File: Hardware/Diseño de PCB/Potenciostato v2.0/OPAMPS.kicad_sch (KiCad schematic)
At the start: 29 parts, among them IC1 LMP7702MAX_NOPB, IC2 LMP7701MFX_NOPB, IC3 LMP7701MFX_NOPB, U1 MAX4737EUD+, U2 LMP7721MA/NOPB, U4 MAX5491LA01000+T, U5 MAX4617CSE+

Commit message: Big commit. Hardware was already ready. Board arrived. Hardware testing phase and software development is ongoing, some hardware issues were detected and noted down in the KiCad project for future versions and design corrections. First software libraries under development for ADC, GPIO, Muxes and DAC managment (ADS1255, MAX5217, MAX4737, MAX4617 and GPIO)
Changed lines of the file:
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@@
 	)
 	(hierarchical_label "CE"
-		(shape input)
+		(shape output)
 		(at 91.44 66.04 180)
 		(fields_autoplaced yes)

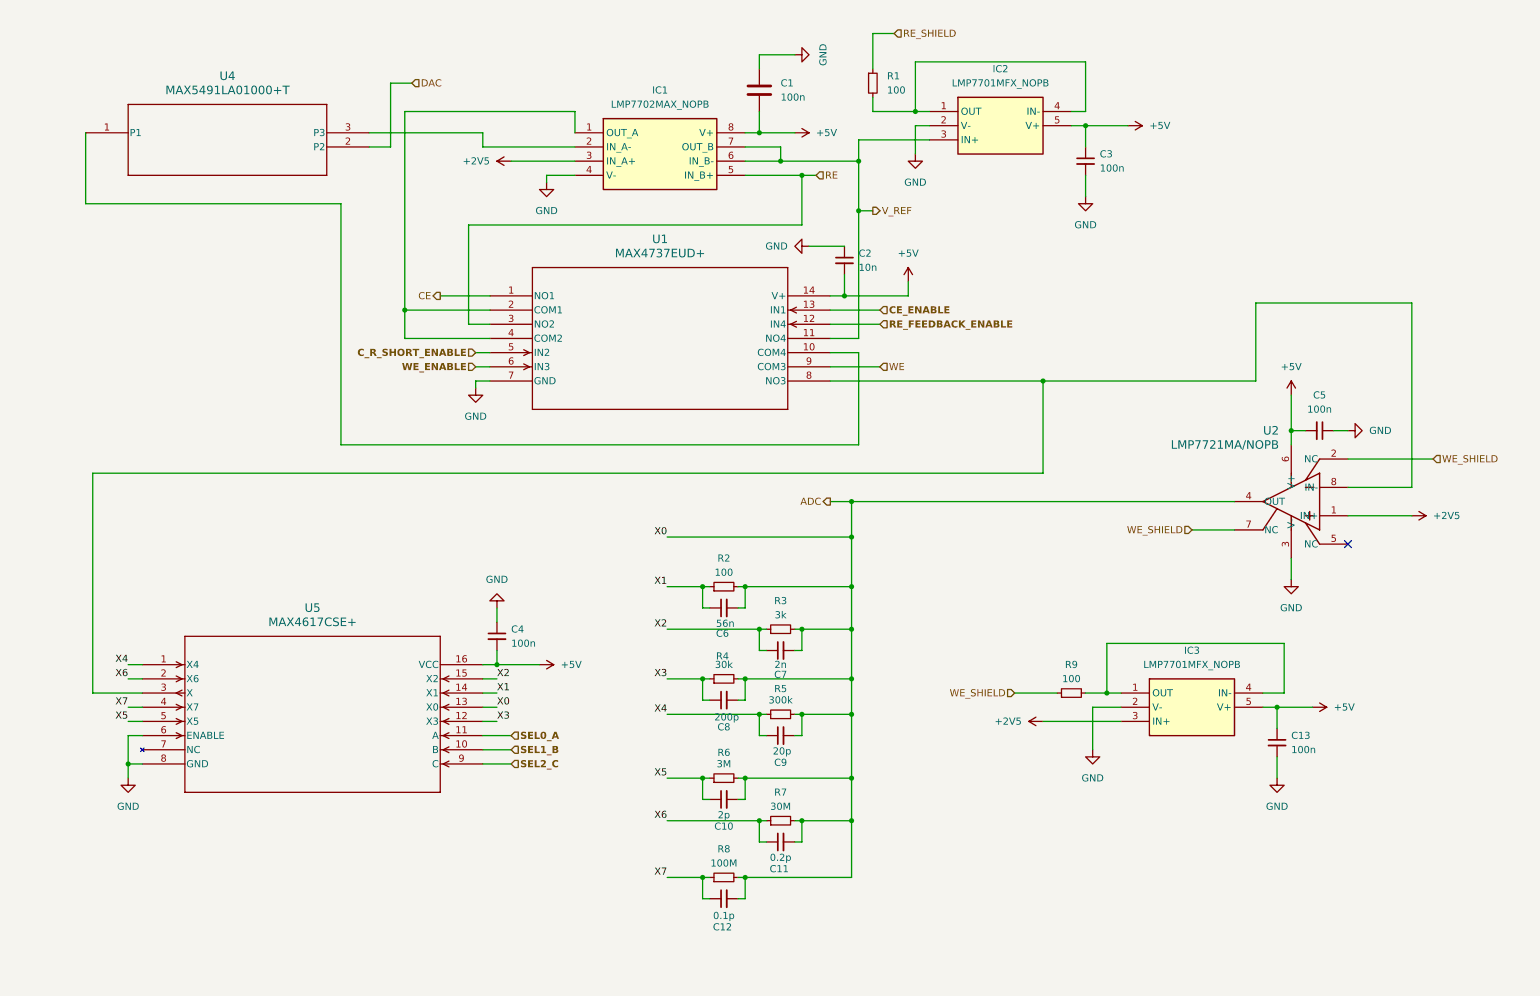
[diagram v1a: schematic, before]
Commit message: Further documentation and notes on the schematic. Software updates: In MAX4617, corrections in write function, more robust code verification to prevent overflows. In MUX, correction to MAX4617 gain codification and pinout updgraded for MAX4737. ADS1255, mux configured to AIN0-AINCOM in ADS_Initialized.
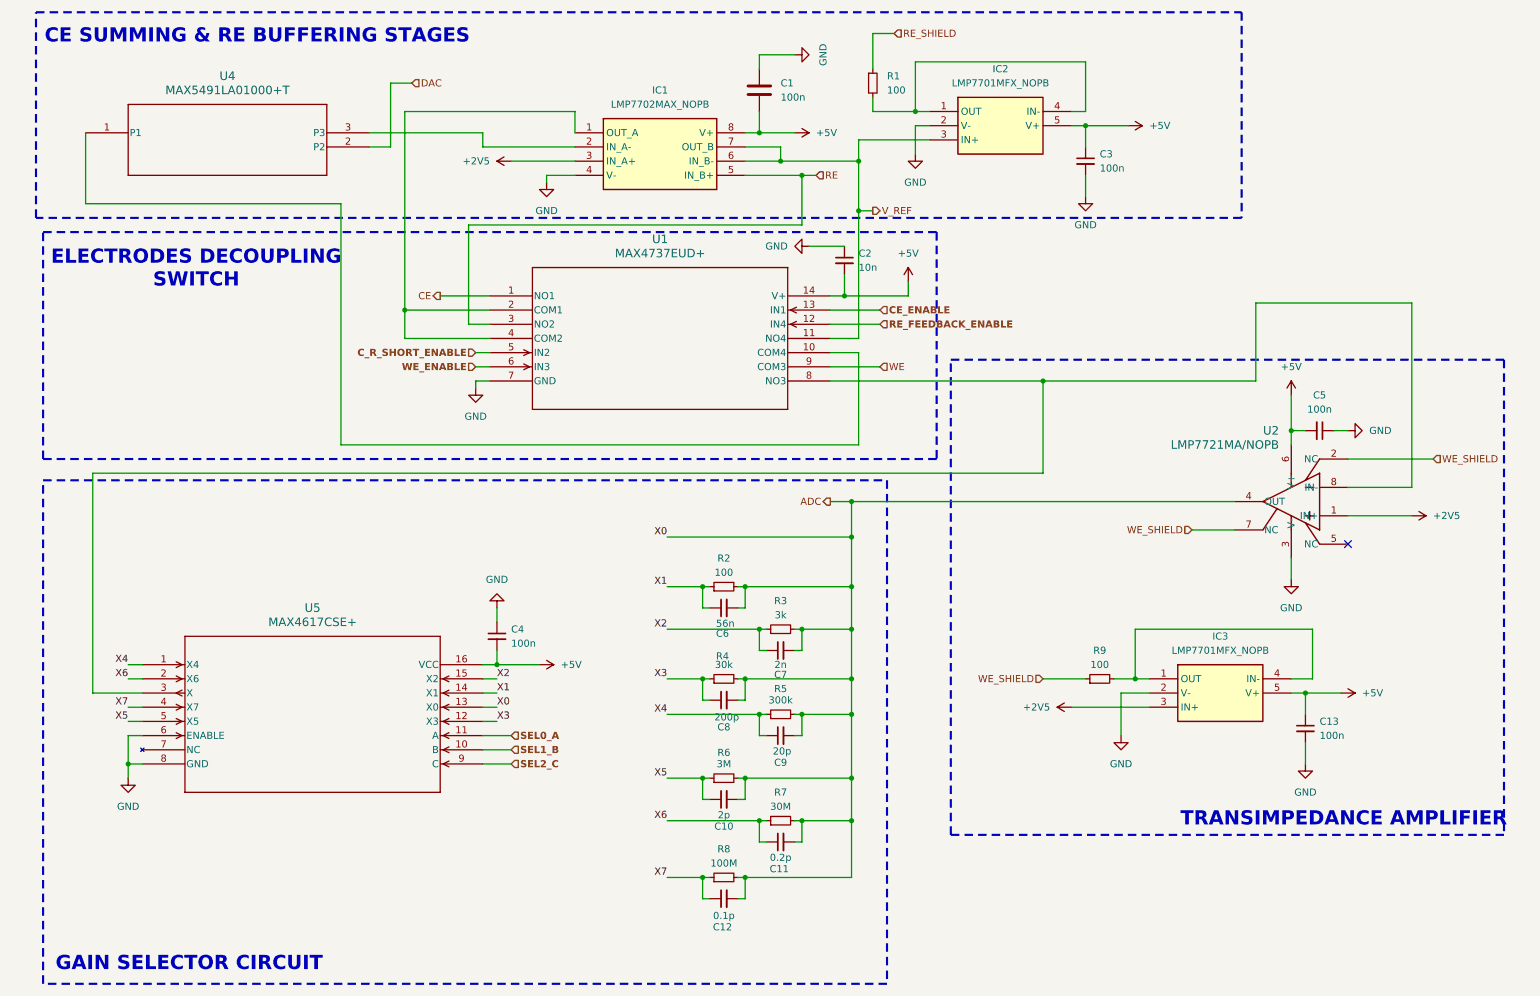
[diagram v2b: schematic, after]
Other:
- note added: "CE SUMMING & RE BUFFERING STAGES"
- note added: "ELECTRODES DECOUPLING SWITCH"
- note added: "GAIN SELECTOR CIRCUIT"
- note added: "TRANSIMPEDANCE AMPLIFIER"
- moved on the sheet: C13, IC3, R9

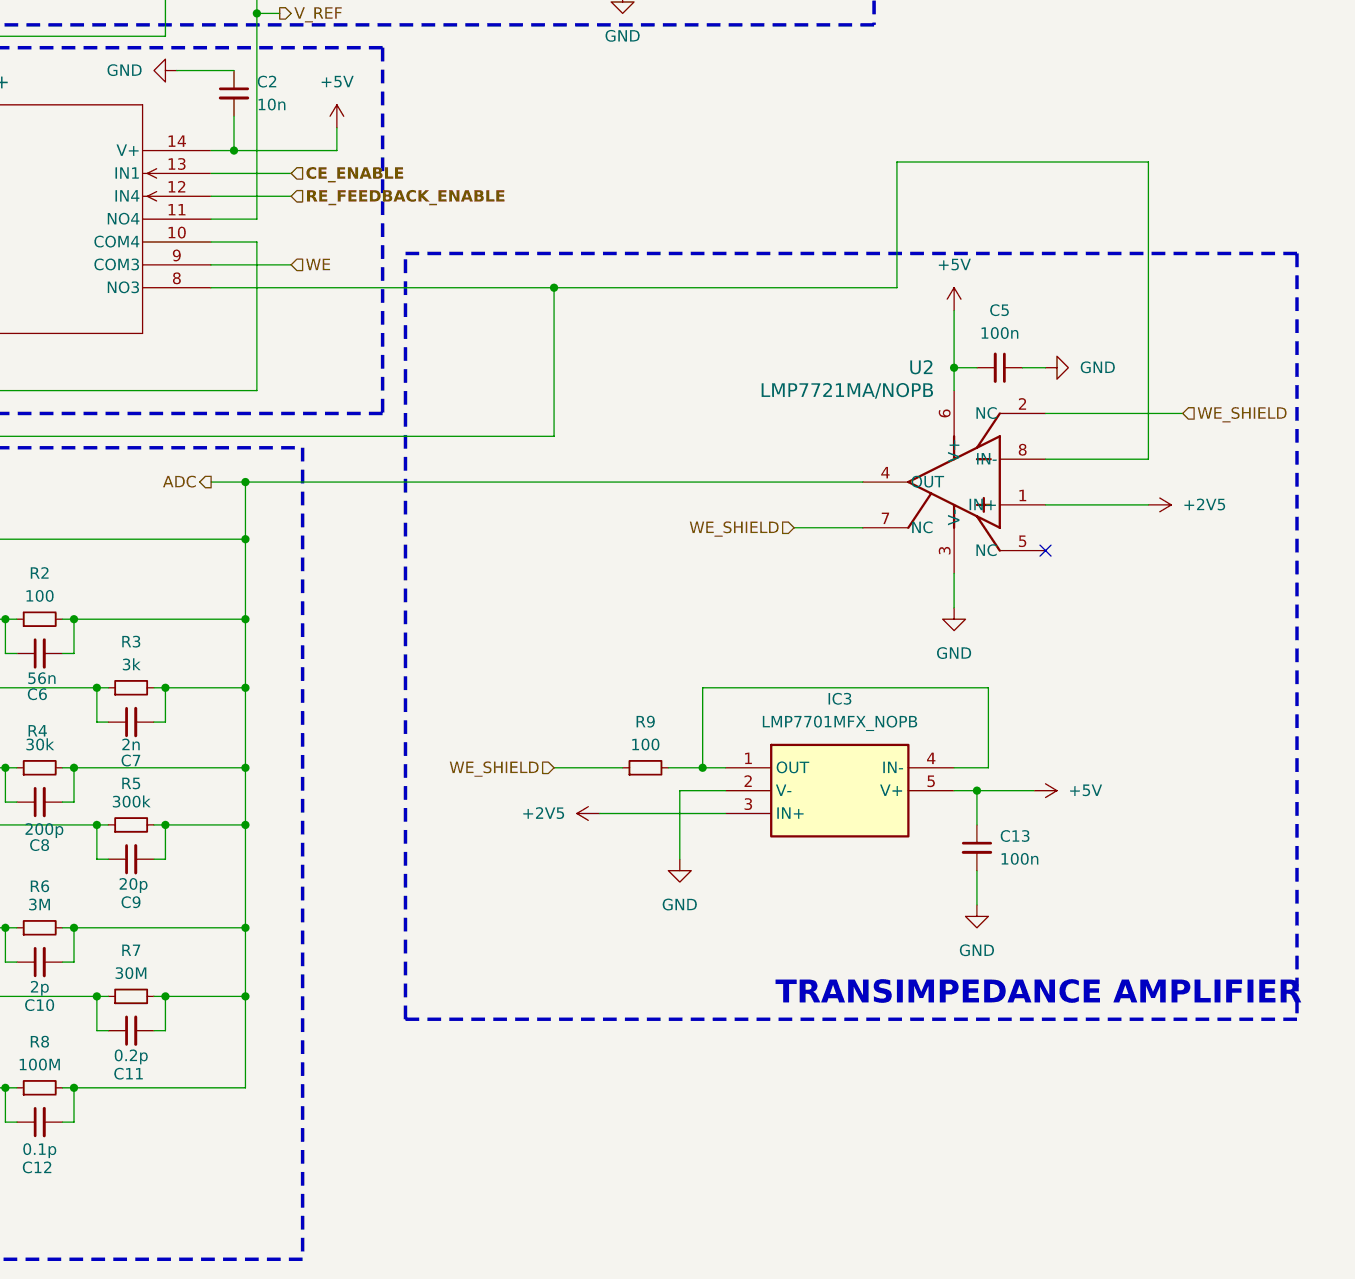
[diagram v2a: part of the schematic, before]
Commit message: Hardware: Hardware Corrections in Potentiostat, small but important ones (WE electrode, Normal Open connection for electric disconnection in schematic and PCB. DAC I2C pull up resistors connected to 5V PCB layout corrected.). New project for ESP32 board: board design to hold ESP32 and LevelShifter for I2C3.3V to 5V. No more. No big changes in firmware and software, nothing to note, really small corrections in that were in the way.
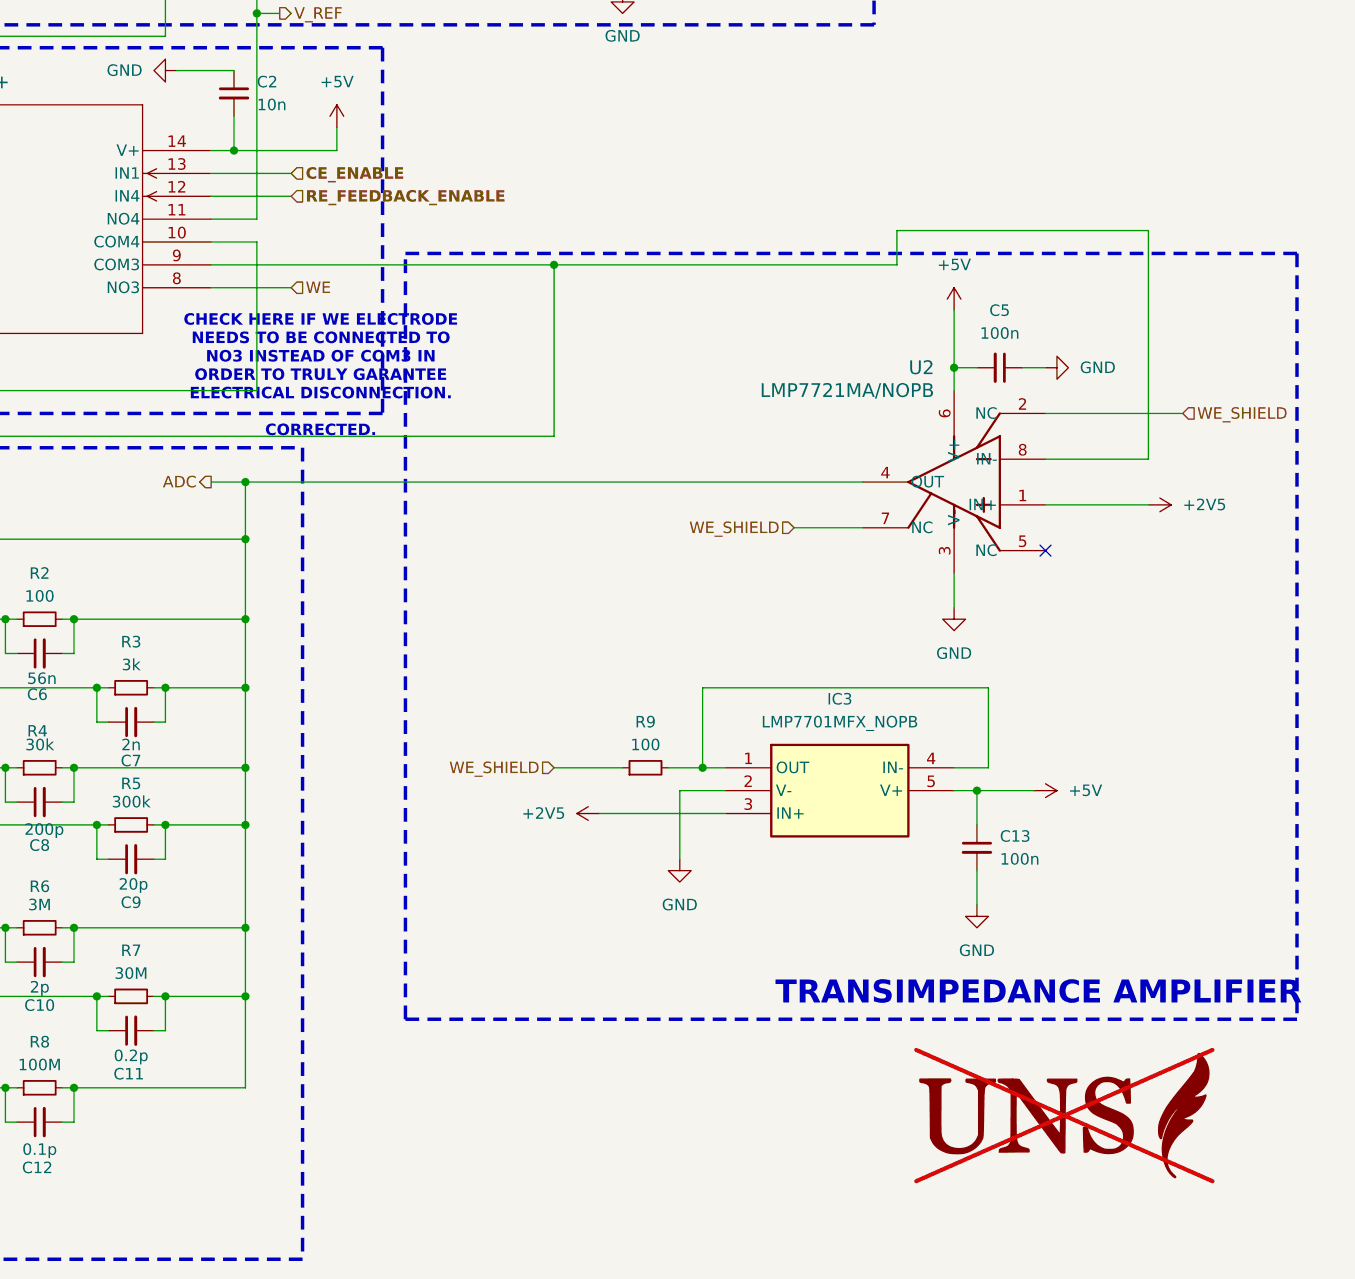
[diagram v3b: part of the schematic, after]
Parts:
- added U9: ~, symbol Graphics_images:UNS_logo
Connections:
- net WE: now also U1.8 (NO3); no longer U1.9 (COM3)
- net at U2.8 (IN-), U5.3 (X): now also U1.9 (COM3); no longer U1.8 (NO3)
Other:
- note added: "CHECK HERE IF WE ELECTRODE NEEDS TO BE CONNECTED TO NO3 INSTEAD OF COM3 IN ORDER TO TRULY GARANTEE ELECTRICAL DISCONNECTION. CORRECTED."
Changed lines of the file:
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@@
 	)
 	(junction
-		(at 199.39 81.28)
+		(at 146.05 118.11)
 		(diameter 0)
 		(color 0 0 0 0)
 	)
 	(junction
-		(at 146.05 118.11)
+		(at 199.39 78.74)
 		(diameter 0)
 		(color 0 0 0 0)
@@
 	(wire
 		(pts
-			(xy 265.43 67.31) (xy 265.43 100.33)
+			(xy 265.43 74.93) (xy 265.43 100.33)
 		)
 		(stroke
@@
 	(wire
 		(pts
-			(xy 237.49 67.31) (xy 265.43 67.31)
+			(xy 237.49 74.93) (xy 265.43 74.93)
 		)
 		(stroke
@@
 	(wire
 		(pts
-			(xy 237.49 81.28) (xy 199.39 81.28)
+			(xy 237.49 78.74) (xy 199.39 78.74)
 		)
 		(stroke
@@
 	(wire
 		(pts
-			(xy 237.49 67.31) (xy 237.49 81.28)
+			(xy 237.49 74.93) (xy 237.49 78.74)
 		)
 		(stroke
@@
 	(wire
 		(pts
+			(xy 199.39 78.74) (xy 199.39 97.79)
+		)
+		(stroke
+			(width 0)
+			(type default)
+		)
+	)
+	(wire
+		(pts
 			(xy 104.14 41.91) (xy 115.57 41.91)
 		)
@@
 	(wire
 		(pts
-			(xy 161.29 78.74) (xy 170.18 78.74)
+			(xy 138.43 173.99) (xy 139.7 173.99)
 		)
 		(stroke
@@
 	(wire
 		(pts
-			(xy 138.43 173.99) (xy 139.7 173.99)
+			(xy 149.86 125.73) (xy 148.59 125.73)
 		)
 		(stroke
@@
 	(wire
 		(pts
-			(xy 149.86 125.73) (xy 148.59 125.73)
+			(xy 161.29 81.28) (xy 170.18 81.28)
 		)
 		(stroke
@@
 	(wire
 		(pts
-			(xy 161.29 81.28) (xy 199.39 81.28)
-		)
-		(stroke
-			(width 0)
-			(type default)
-		)
-	)
-	(wire
-		(pts
 			(xy 148.59 129.54) (xy 149.86 129.54)
 		)
@@
 	(wire
 		(pts
-			(xy 199.39 81.28) (xy 199.39 97.79)
+			(xy 132.08 109.22) (xy 165.1 109.22)
 		)
 		(stroke
@@
 	(wire
 		(pts
-			(xy 132.08 109.22) (xy 165.1 109.22)
+			(xy 35.56 149.86) (xy 38.1 149.86)
 		)
 		(stroke
@@
 	(wire
 		(pts
-			(xy 35.56 149.86) (xy 38.1 149.86)
+			(xy 146.05 118.11) (xy 146.05 121.92)
 		)
 		(stroke
@@
 	(wire
 		(pts
-			(xy 146.05 118.11) (xy 146.05 121.92)
+			(xy 168.91 33.02) (xy 176.53 33.02)
 		)
 		(stroke
@@
 	(wire
 		(pts
-			(xy 168.91 33.02) (xy 176.53 33.02)
+			(xy 99.06 149.86) (xy 104.14 149.86)
 		)
 		(stroke
@@
 	(wire
 		(pts
-			(xy 99.06 149.86) (xy 104.14 149.86)
+			(xy 226.06 107.95) (xy 233.68 107.95)
 		)
 		(stroke
@@
 	(wire
 		(pts
-			(xy 226.06 107.95) (xy 233.68 107.95)
+			(xy 163.83 66.04) (xy 175.26 66.04)
 		)
 		(stroke
@@
 	(wire
 		(pts
-			(xy 163.83 66.04) (xy 175.26 66.04)
+			(xy 161.29 78.74) (xy 199.39 78.74)
 		)
 		(stroke
@@
 		)
 	)
+	(text "CHECK HERE IF WE ELECTRODE\nNEEDS TO BE CONNECTED TO\nNO3 INSTEAD OF COM3 IN \nORDER TO TRULY GARANTEE\nELECTRICAL DISCONNECTION.\n\nCORRECTED.\n\n"
+		(exclude_from_sim no)
+		(at 173.482 92.202 0)
+		(effects
+			(font
+				(size 1.27 1.27)
+				(thickness 0.254)
+				(bold yes)
+				(color 255 0 4 1)
+			)
+		)
+	)
 	(text "TRANSIMPEDANCE AMPLIFIER"
 		(exclude_from_sim no)
@@
 	(hierarchical_label "WE"
 		(shape input)
-		(at 170.18 78.74 0)
+		(at 170.18 81.28 0)
 		(fields_autoplaced yes)
 		(effects
@@
 					(unit 1)
 				)
+			)
+		)
+	)
+	(symbol
+		(lib_id "Graphics_images:UNS_logo")
+		(at 240.03 166.37 0)
+		(unit 1)
+		(exclude_from_sim no)
+		(in_bom no)
+		(on_board no)
+		(dnp yes)
+		(fields_autoplaced yes)
+		(property "Reference" "U9"
+			(at 239.268 161.798 0)
+			(effects
+				(font
+					(size 1.27 1.27)
+				)
+				(justify left)
+				(hide yes)
+			)
+		)
+		(property "Value" "~"
+			(at 219.71 157.48 0)
+			(effects
+				(font
+					(size 1.27 1.27)
+				)
+				(justify left)
+			)
+		)
+		(property "Footprint" ""
+			(at 231.14 162.56 0)
+			(effects
+				(font
+					(size 1.27 1.27)
+				)
+				(hide yes)
+			)
+		)
+		(property "Datasheet" ""
+			(at 231.14 162.56 0)
+			(effects
+				(font
+					(size 1.27 1.27)
+				)
+				(hide yes)
+			)
+		)
+		(property "Description" ""
+			(at 231.14 162.56 0)
+			(effects
+				(font
+					(size 1.27 1.27)
+				)
+				(hide yes)
+			)
+		)
+		(property "JLCLIB" ""
+			(at 240.03 166.37 0)
+			(effects
+				(font
+					(size 1.27 1.27)
+				)
+				(hide yes)
+			)
+		)
+		(instances
+			(project "Potenciostato v2.0"
+				(path "/3273751a-bb69-4014-b380-866ff743e010/5d79f500-565e-419c-88c4-671a7a05adc5"
+					(reference "U9")
+					(unit 1)
+				)
